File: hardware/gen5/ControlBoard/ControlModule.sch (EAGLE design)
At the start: 40 parts, among them IC1 XMEGA16A4A

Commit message: deleted unneccessary signals
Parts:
- removed R2, R3, R4: 4.7k, SparkFun-Resistors:RESISTOR0805-RES
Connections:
- removed net BB_IN: IC1.PA0, JP1.7
- removed net DISCHARGE: IC1.PB2, JP1.16
- removed net DIVCAP: IC1.PA2, JP1.14
- removed net DRIB: IC1.PA3, JP1.18
- removed net N$1: JP1.32, R2.2
- removed net N$3: JP1.30, R3.2
- removed net N$8: JP1.28, R4.2
- new net N$4: JP1.39, JP1.40
- new net N$6: JP1.37, JP1.38
- net 12VGND: no longer 3.3REG.GND, C4.2, C5.2, C6.2, JP1.37, JP1.38, JP1.39, JP1.40, U$2.P$1
- net BB_OUT: no longer JP1.9
- net CHARGE: no longer JP1.19
- net CHARGE_DONE: no longer JP1.17
- net CHIP_ENABLE: no longer JP1.13
- net GND: now also 3.3REG.GND, C4.2, C5.2, C6.2, U$2.P$1
- net KICK_ENABLE: no longer JP1.11
- net KICK_REF: no longer JP1.15
- net MISO: no longer R2.1
- net MOSI: no longer R3.1
- net SCK: no longer R4.1
- net SS_1: no longer JP1.20
- net SS_2: no longer JP1.22
- net SS_3: no longer JP1.24
- net SS_4: no longer JP1.26
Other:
- note added: "We need to add the I2C lines here"

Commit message: Added fault signals to main board. Need to add an OR gate to OR them together before connecting them to the MCU
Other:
- note added: "Also, we definitely do not need a 40 pin connector"
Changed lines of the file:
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@@
 <plain>
 <text x="45.72" y="157.48" size="1.778" layer="99">We need to add the I2C lines here</text>
+<text x="45.72" y="152.4" size="1.778" layer="99">Also, we definitely do not need a 40 pin connector</text>
 </plain>
 <instances>

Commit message: finished control module - needs review - might need more condensing?
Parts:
- removed 3.3V: TEST_PT, gen3:TEST_PT
- removed C1: 1uF, SparkFun-Capacitors:CAP0805
- removed C2: 0.01uF, SparkFun-Capacitors:CAP0805
- removed C3: 0.1uF, SparkFun-Capacitors:CAP0805
- removed IC1: XMEGA16A4A, atmel:XMEGA16A4A
- removed JP1: M20X2SHROUDED_SMT, SparkFun-Connectors:M20X2SHROUDED_SMT
- removed JP3: DEBUG, pinhead:PINHD-2X5
- removed LED2, LED3, LED9: (no value), SparkFun-LED:LED1206
- removed S1, S3: TAC_SWITCHSMD, SparkFun-Retired:TAC_SWITCHSMD
- added C14, C9: 0.1uF, SparkFun-Capacitors:CAP0805
- added C8: 10uF, SparkFun-Capacitors:CAP0805
- added PWR_LED, RX_LED, SCK_LED: (no value), SparkFun-LED:LED1206
- added Q1, Q2: BSS123, transistor-small-signal:BSS123
- added R10: 100, SparkFun-Passives:RESISTOR0805-RES
- added R2, R5: 10k, SparkFun-Passives:RESISTOR0805-RES
- added R3, R4: 0, SparkFun-Passives:RESISTOR0805-RES
- added S2, S4: TAC_SWITCHSMD, SparkFun-Retired:TAC_SWITCHSMD
- added SV1: ICSP, con-lstb:MA03-2
- added SV2, SV3: (no value), con-lstb:MA10-1W
- added U1: ATMEGA328P-AU, Atmel_By_element14_Batch_1-00:ATMEGA328P-AU
- R1, R7: value 10k -> 100
- R6: value 4.7k -> 100
- R8: value 80.6k -> 10k
- R9: value 20k -> 10k
- renumbered LED1 to TX_LED
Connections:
- removed net AVCC: C3.2, IC1.AVCC, R1.1
- removed net BATSENSE: IC1.PA1, R8.1, R9.2
- removed net BB_OUT: IC1.PB0
- removed net CHARGE: IC1.PB3
- removed net CHARGE_DONE: IC1.PB1
- removed net CHIP_ENABLE: IC1.PC3
- removed net DATA: IC1.PDI_DATA, JP3.9
- removed net GLED1: IC1.PR0(XT2), R13.2
- removed net GLED2: IC1.PD1, R15.2
- removed net KICK_ENABLE: IC1.PC4
- removed net KICK_REF: IC1.PD0
- removed net N$4: JP1.39, JP1.40
- removed net N$6: JP1.37, JP1.38
- removed net RESET: IC1.!RESET!/PDI_CLK, JP3.6, R7.1, S3.4
- removed net RLED1: IC1.PR1(XT1), R14.2
- removed net RLED2: IC1.PD2, R16.2
- removed net SS_1: IC1.PA7
- removed net SS_2: IC1.PA6
- removed net SS_3: IC1.PA5
- removed net SS_4: IC1.PA4
- new net N$1: R3.2, XBEE.RTS
- new net N$12: Q2.G, R10.2, R8.2, S4.3, S4.4
- new net N$13: Q1.G, R7.1, R9.1, S2.1, S2.2
- new net N$3: R4.2, XBEE.CTS
- new net N$7: R10.1, U1.PC0
- new net N$8: R6.1, U1.PC5
- new net RST: Q1.D, R2.1, SV1.5, U1.PC6
- new net RST_CTRL: R7.2, SV2.4
- new net TWCK: R6.2, SV2.5
- new net TWD: R1.2, SV2.6
- net 12V: now also SV2.10, SV2.8, SV2.9; no longer JP1.1, JP1.2, JP1.3, JP1.4, JP1.5, JP1.6, R8.2
- net 12VGND: now also 3.3REG.GND, C4.2, C5.2, C6.2, SV2.1, SV2.2, SV2.3, U$2.P$1; no longer JP1.35, JP1.36
- net 3.3V: now also C14.1, C8.1, C9.1, R16.2, R2.2, R5.2, S2.3, S2.4, S4.1, S4.2, SV1.2, U1.AREF, U1.AVCC, U1.VCC, U1.VCC_2; no longer 3.3V.P$1, C1.1, C2.1, IC1.VCC, IC1.VCC1, IC1.VCC2, JP3.4, R1.2, R7.2
- net BID0: now also U1.PB7; no longer IC1.PE0
- net BID1: now also U1.PD5; no longer IC1.PE1
- net BID2: now also U1.PD6; no longer IC1.PE2
- net BID3: now also U1.PD7; no longer IC1.PE3
- net CTS: now also R4.1, U1.PD3; no longer IC1.PD4, XBEE.CTS
- net GND: now also C14.2, C8.2, C9.2, PWR_LED.C, Q1.S, Q2.S, R8.1, R9.2, RX_LED.C, SCK_LED.C, SV1.6, U1.GND, U1.GND_2, U1.GND_3; no longer 3.3REG.GND, C1.2, C2.2, C3.1, C4.2, C5.2, C6.2, IC1.GND, IC1.GND1, IC1.GND2, IC1.GND3, JP1.33, JP1.34, JP3.10, LED2.C, LED3.C, LED9.C, R9.1, S1.2, S3.2, U$2.P$1
- net MISO: now also SV1.1, U1.PB4; no longer IC1.PC6
- net MOSI: now also SV1.4, U1.PB3; no longer IC1.PC5
- net N$10: now also RX_LED.A; no longer LED2.A
- net N$11: now also PWR_LED.A; no longer LED3.A
- net N$2: now also SCK_LED.A; no longer LED9.A
- net N$5: now also R1.1, U1.PC4; no longer IC1.PD3, R6.1
- net RTS: now also R3.1, U1.PD2; no longer IC1.PD5, XBEE.RTS
- net RX: now also R15.2, U1.PD0; no longer IC1.PD6
- net SCK: now also R13.2, SV1.3, U1.PB5; no longer IC1.PC7
- net TX: now also R14.2, U1.PD1; no longer IC1.PD7
- net XBRST: now also Q2.D, R5.1; no longer R6.2, S1.4
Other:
- note added: "RTS/CTS likely not necessary, but can be connected if needed."
- note removed: "Also, we definitely do not need a 40 pin connector"
- note removed: "We need to add the I2C lines here"
- moved on the sheet: C11, C12, R1, R13, R15, R16, R6, R7, R8, R9, RX, TX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

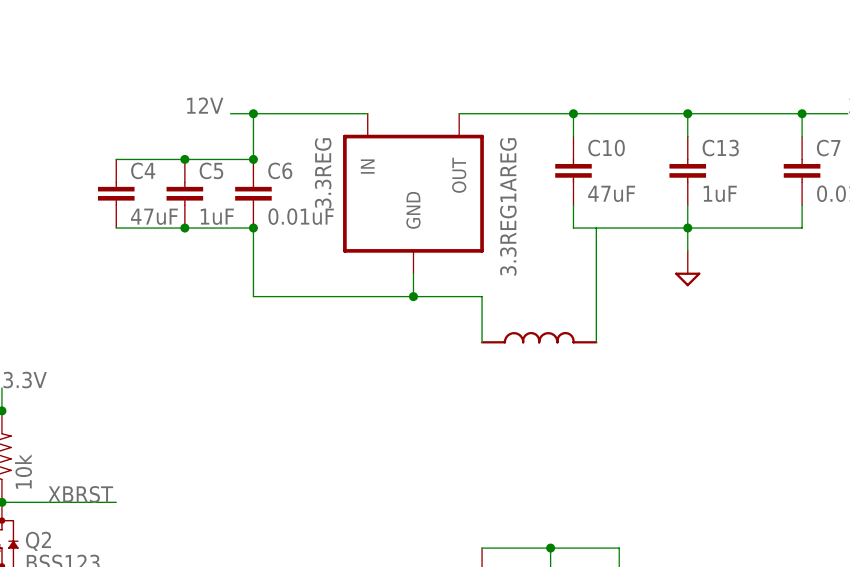
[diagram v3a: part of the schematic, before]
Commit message: small fix to control module gnd
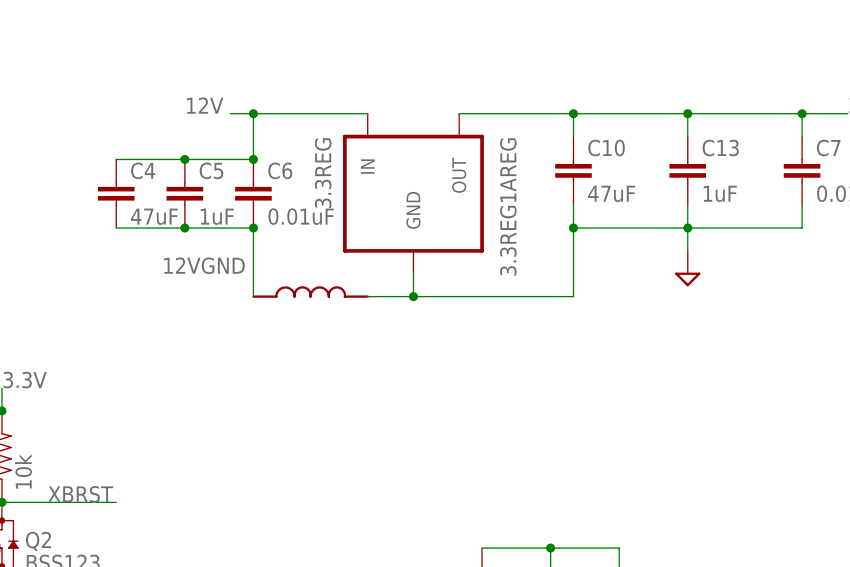
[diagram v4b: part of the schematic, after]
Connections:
- net 12VGND: no longer 3.3REG.GND
- net GND: now also 3.3REG.GND
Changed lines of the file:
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@@
 <instance part="C5" gate="G$1" x="111.76" y="132.08"/>
 <instance part="C6" gate="G$1" x="119.38" y="132.08"/>
-<instance part="U$2" gate="G$1" x="144.78" y="116.84"/>
+<instance part="U$2" gate="G$1" x="119.38" y="121.92"/>
 <instance part="U1" gate="A" x="53.34" y="68.58"/>
 <instance part="C8" gate="G$1" x="10.16" y="86.36"/>
@@
 <pinref part="C13" gate="G$1" pin="2"/>
 <wire x1="167.64" y1="132.08" x2="167.64" y2="129.54" width="0.1524" layer="91"/>
-<wire x1="167.64" y1="129.54" x2="157.48" y2="129.54" width="0.1524" layer="91"/>
+<wire x1="167.64" y1="129.54" x2="154.94" y2="129.54" width="0.1524" layer="91"/>
 <pinref part="C7" gate="G$1" pin="2"/>
 <wire x1="180.34" y1="132.08" x2="180.34" y2="129.54" width="0.1524" layer="91"/>
@@
 <wire x1="167.64" y1="129.54" x2="167.64" y2="127" width="0.1524" layer="91"/>
 <pinref part="C10" gate="G$1" pin="2"/>
+<pinref part="SUPPLY7" gate="GND" pin="GND"/>
 <pinref part="U$2" gate="G$1" pin="P$2"/>
-<wire x1="154.94" y1="129.54" x2="157.48" y2="129.54" width="0.1524" layer="91"/>
-<wire x1="157.48" y1="129.54" x2="157.48" y2="116.84" width="0.1524" layer="91"/>
-<pinref part="SUPPLY7" gate="GND" pin="GND"/>
+<pinref part="3.3REG" gate="G$1" pin="GND"/>
+<wire x1="132.08" y1="121.92" x2="137.16" y2="121.92" width="0.1524" layer="91"/>
+<wire x1="137.16" y1="121.92" x2="137.16" y2="124.46" width="0.1524" layer="91"/>
+<wire x1="137.16" y1="121.92" x2="154.94" y2="121.92" width="0.1524" layer="91"/>
+<wire x1="154.94" y1="121.92" x2="154.94" y2="129.54" width="0.1524" layer="91"/>
+<junction x="137.16" y="121.92"/>
+<junction x="154.94" y="129.54"/>
 </segment>
 <segment>
@@
 <net name="12VGND" class="0">
 <segment>
-<pinref part="3.3REG" gate="G$1" pin="GND"/>
-<wire x1="119.38" y1="121.92" x2="137.16" y2="121.92" width="0.1524" layer="91"/>
-<wire x1="137.16" y1="121.92" x2="137.16" y2="124.46" width="0.1524" layer="91"/>
 <pinref part="C6" gate="G$1" pin="2"/>
 <wire x1="119.38" y1="121.92" x2="119.38" y2="129.54" width="0.1524" layer="91"/>
@@
 <junction x="119.38" y="129.54"/>
 <pinref part="U$2" gate="G$1" pin="P$1"/>
-<wire x1="137.16" y1="121.92" x2="144.78" y2="121.92" width="0.1524" layer="91"/>
-<wire x1="144.78" y1="121.92" x2="144.78" y2="116.84" width="0.1524" layer="91"/>
-<junction x="137.16" y="121.92"/>
-</segment>
-<segment>
+<label x="109.22" y="124.46" size="1.778" layer="95"/>
+</segment>
+<segment>
